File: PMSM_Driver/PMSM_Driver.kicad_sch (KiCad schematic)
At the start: 112 parts, among them J1 Screw_Terminal_01x03, J2 Screw_Terminal_01x12, Q1 RGCL60TK60, Q10 RGCL60TK60, Q11 RGCL60TK60, Q12 RGCL60TK60, Q2 RGCL60TK60, Q3 RGCL60TK60, Q4 RGCL60TK60, Q5 RGCL60TK60, Q6 RGCL60TK60, Q7 RGCL60TK60, Q8 RGCL60TK60, Q9 RGCL60TK60, U1 HCPL-3120, U10 HCPL-3120, U11 HCPL-3120, U12 HCPL-3120, U2 HCPL-3120, U3 HCPL-3120, U4 HCPL-3120, U5 HCPL-3120, U6 HCPL-3120, U7 HCPL-3120, U8 HCPL-3120, U9 HCPL-3120

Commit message: modified the schematic and PCB layout, updated datasheet and BOM
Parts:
- removed C14: 10n, Capacitor_SMD:C_0402_1005Metric, symbol Device:C_Polarized_Small
- removed C15, C18: 0.1u, Capacitor_SMD:C_0402_1005Metric, symbol Device:C_Polarized_Small
- removed D1, D13, D14, D2, D7, D8: DIODE, Package_TO_SOT_SMD:TO-263-2, symbol pspice:DIODE
- removed D10, D11, D12, D15, D16, D17, D18, D3, D4, D5, D6, D9: DIODE, Package_TO_SOT_SMD:TO-263-2, symbol Simulation_SPICE:DIODE
- removed J2: Screw_Terminal_01x12, TerminalBlock_Phoenix:TerminalBlock_Phoenix_PT-1,5-12-3.5-H_1x12_P3.50mm_Horizontal, symbol Connector:Screw_Terminal_01x12
- removed R4, R5: 500, Resistor_SMD:R_0603_1608Metric, symbol Device:R_Small
- removed R7: 10, Resistor_SMD:R_0603_1608Metric, symbol Device:R_Small
- removed U1, U11, U2, U5, U6, U7, U8, U9: HCPL-3120, Package_DIP:DIP-8_W7.62mm_SMDSocket_SmallPads, symbol Driver_FET:HCPL-3120
- added C1, C10, C2, C27, C28, C29, C30, C31, C32, C33, C34, C35, C36, C37, C38, C39, C40, C41, C42, C43, C44, C45, C46, C47, C48, C49, C50, C51, C52, C53, C54, C55, C56, C57, C58, C59, C60, C61, C62, C63, C64, C65, C66, C67, C68, C69, C70, C71, C72, C73, C74, C75, C76, C77, C78, C79, C80, C81: 1u, Capacitor_SMD:C_0402_1005Metric, symbol Device:C_Polarized_Small
- added C82, C83, C84: 1n, Capacitor_SMD:C_0603_1608Metric, symbol Device:C_Polarized
- added C85, C86, C87: 0.1u, Capacitor_SMD:C_0402_1005Metric, symbol Device:C_Polarized_Small
- added J10, J11, J12, J13, J14, J15, J16, J2, J6, J7, J8, J9: AFBR-2624Z, OptoDevice:Broadcom_AFBR-16xxZ_Horizontal, symbol Fiber_Optic:AFBR-2624Z
- added J17, J18, J5: AFBR-1624Z, OptoDevice:Broadcom_AFBR-16xxZ_Horizontal, symbol Fiber_Optic:AFBR-1624Z
- added J3: Screw_Terminal_01x02, FYP_Components:8PCV-02-006, symbol Connector:Screw_Terminal_01x02
- added J4: Screw_Terminal_01x02, TerminalBlock_Phoenix:TerminalBlock_Phoenix_MKDS-1,5-2-5.08_1x02_P5.08mm_Horizontal, symbol Connector:Screw_Terminal_01x02
- added Q1, Q10, Q15, Q2, Q20, Q21, Q22, Q23, Q24, Q3, Q4, Q9: BC846, Package_TO_SOT_SMD:SOT-23, symbol Transistor_BJT:BC846
- added R1, R2, R6: 270, Resistor_SMD:R_0603_1608Metric, symbol Device:R_Small
- added R39, R40, R41: 4.7k, Resistor_SMD:R_0402_1005Metric, symbol Device:R_Small
- added U1, U13, U14, U15, U22, U23, U24, U31, U32, U4, U5, U6: 74LVC1G04, Package_TO_SOT_SMD:SOT-23-5, symbol 74xGxx:74LVC1G04
- added U16, U17, U18, U2, U25, U26, U27, U33, U34, U7, U8, U9: MGJ2D051515SC, Converter_DCDC:Converter_DCDC_Murata_MGJ2DxxxxxxSC_THT, symbol Converter_DCDC:MGJ2D051515SC
- added U19, U20, U21, U28, U29, U30, U35, U36: HCPL-3120, Package_DIP:DIP-8_W8.89mm_SMDSocket_LongPads, symbol Driver_FET:HCPL-3120
- added U37, U38, U39, U40, U41, U42, U43, U44, U45, U46, U47, U48, U49, U50, U51, U52, U53, U54: VS-E5TH3006S2L-M3, Package_TO_SOT_SMD:TO-263-2, symbol FYP_Components:VS-E5TH3006S2L-M3
- added U55, U56, U57: ACS723xLCTR-40AB, Package_SO:SOIC-8_3.9x4.9mm_P1.27mm, symbol Sensor_Current:ACS723xLCTR-40AB
- C11, C12, C13, C19, C20, C21, C22, C4, C6: value 10n -> 1u
- C14: renamed from C1; value 4.7u -> 22u; footprint Capacitor_SMD:CP_Elec_10x10.5 -> Capacitor_SMD:CP_Elec_16x17.5
- C15: renamed from C2; value 4.7u -> 22u; footprint Capacitor_SMD:CP_Elec_10x10.5 -> Capacitor_SMD:CP_Elec_16x17.5
- C16, C17, C23, C24, C25, C26, C7, C8, C9: value 0.1u -> 1u
- C18: renamed from C10; value 0.1u -> 1u
- C3, C5: value 10n -> 0.1u
- R10, R19, R20, R33, R34, R8, R9: value 10 -> 270
- R11, R24, R25, R26, R35, R36: value 1000 -> 270; footprint Resistor_SMD:R_1206_3216Metric -> Resistor_SMD:R_0603_1608Metric
- R12, R13, R14, R23, R37, R38: value 1000 -> 10; footprint Resistor_SMD:R_1206_3216Metric -> Resistor_SMD:R_0603_1608Metric
- R15, R16, R17, R18, R27, R28, R29: value 500 -> 270
- R3, R30: value 500 -> 10
- R7: renamed from R6; value 500 -> 270
- U10, U12, U3: footprint Package_DIP:DIP-8_W7.62mm_SMDSocket_SmallPads -> Package_DIP:DIP-8_W8.89mm_SMDSocket_LongPads
- U11: renamed from U4; footprint Package_DIP:DIP-8_W7.62mm_SMDSocket_SmallPads -> Package_DIP:DIP-8_W8.89mm_SMDSocket_LongPads
- renumbered Q5 to Q11, Q6 to Q12, Q7 to Q13, Q8 to Q14, Q9 to Q16, Q10 to Q17, Q11 to Q18, Q12 to Q19, Q1 to Q5, Q2 to Q6, Q3 to Q7, Q4 to Q8, R1 to R4, R2 to R5
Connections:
- net +BATT: now also J3.1 (Pin_1), U43.2 (C), U47.2 (C), U51.2 (C)
- net -BATT: now also C57.2, C63.2, C69.2, C71.2, C73.2, C75.2, C77.2, C79.2, C81.2, J3.2 (Pin_2), U27.5 (-VOUT), U30.5 (VEE), U33.5 (-VOUT), U34.5 (-VOUT), U35.5 (VEE), U36.5 (VEE), U46.1 (N/C), U46.3 (A), U50.1 (N/C), U50.3 (A), U54.1 (N/C), U54.3 (A)
- net A1: now also Q5.1 (G), R13.2; no longer R10.2, R14.1, U11.6 (VO), U11.7 (VO)
- net A2: now also Q6.1 (G), R22.2; no longer R13.1, R9.2, U3.6 (VO), U3.7 (VO)
- net A3: now also Q7.1 (G), R31.2; no longer R11.1, R8.2
- net A4: now also Q8.1 (G), R38.2; no longer R12.1
- net B1: now also Q11.1 (G), R12.2; no longer R22.2, R24.1
- net B2: now also Q12.1 (G); no longer R23.1
- net B3: now also Q13.1 (G), R30.2; no longer R20.2, R25.1
- net B4: now also Q14.1 (G), R37.2; no longer R19.2, R26.1
- net C1: now also Q16.1 (G), R3.2; no longer R34.2, R36.1, U12.6 (VO), U12.7 (VO)
- net C2: now also Q17.1 (G), R14.2; no longer R33.2, R37.1
- net C3: now also Q18.1 (G), R23.2; no longer R32.2, R38.1, U10.6 (VO), U10.7 (VO)
- net C4: now also Q19.1 (G), R32.2; no longer R31.2, R35.1
- net GND: now also C1.2, C2.2, C82.2, C83.2, C84.2, C85.2, C86.2, C87.2, J10.2 (VEER), J10.5 (HP), J10.8 (HP), J11.2 (VEER), J11.5 (HP), J11.8 (HP), J12.2 (VEER), J12.5 (HP), J12.8 (HP), J13.2 (VEER), J13.5 (HP), J13.8 (HP), J14.2 (VEER), J14.5 (HP), J14.8 (HP), J15.2 (VEER), J15.5 (HP), J15.8 (HP), J16.2 (VEER), J16.5 (HP), J16.8 (HP), J17.3 (VEET), J17.5 (HP), J17.8 (HP), J18.3 (VEET), J18.5 (HP), J18.8 (HP), J2.2 (VEER), J2.5 (HP), J2.8 (HP), J4.2 (Pin_2), J5.3 (VEET), J5.5 (HP), J5.8 (HP), J6.2 (VEER), J6.5 (HP), J6.8 (HP), J7.2 (VEER), J7.5 (HP), J7.8 (HP), J8.2 (VEER), J8.5 (HP), J8.8 (HP), J9.2 (VEER), J9.5 (HP), J9.8 (HP), R39.2, R40.2, R41.2, U1.3 (GND), U13.3 (GND), U14.3 (GND), U15.3 (GND), U16.2 (-VIN), U17.2 (-VIN), U18.2 (-VIN), U2.2 (-VIN), U22.3 (GND), U23.3 (GND), U24.3 (GND), U25.2 (-VIN), U26.2 (-VIN), U27.2 (-VIN), U31.3 (GND), U32.3 (GND), U33.2 (-VIN), U34.2 (-VIN), U4.3 (GND), U5.3 (GND), U55.5 (GND), U55.6 (BW_SEL), U56.5 (GND), U56.6 (BW_SEL), U57.5 (GND), U57.6 (BW_SEL), U6.3 (GND), U7.2 (-VIN), U8.2 (-VIN), U9.2 (-VIN); no longer C11.2, C12.2, C13.2, C16.2, C17.2, C18.2, C19.2, C20.2, C21.2, C22.2, C23.2, C24.2, C25.2, C26.2, C7.2, C8.2, U10.5 (VEE), U11.5 (VEE), U12.5 (VEE), U3.5 (VEE)
- net GNDD: now also Q1.2 (E), Q10.2 (E), Q15.2 (E), Q2.2 (E), Q20.2 (E), Q21.2 (E), Q22.2 (E), Q23.2 (E), Q24.2 (E), Q3.2 (E), Q4.2 (E), Q9.2 (E), U19.3 (C), U20.3 (C), U21.3 (C), U28.3 (C), U29.3 (C), U30.3 (C), U35.3 (C), U36.3 (C)
- net GNDREF: now also U37.1 (N/C), U37.3 (A), U38.2 (C), U39.1 (N/C), U39.3 (A), U40.2 (C), U41.1 (N/C), U41.3 (A), U42.2 (C)
- net ia_out: now also C37.2, C41.2, C47.2, U17.5 (-VOUT), U20.5 (VEE), U44.1 (N/C), U44.3 (A), U45.2 (C), U55.1 (IP+), U55.2 (IP+); no longer J1.3 (Pin_3)
- net ib_out: now also C35.2, C39.2, C45.2, U16.5 (-VOUT), U19.5 (VEE), U48.1 (N/C), U48.3 (A), U49.2 (C), U56.1 (IP+), U56.2 (IP+); no longer J1.2 (Pin_2)
- net ic_out: now also C21.2, U12.5 (VEE), C27.2, C33.2, U52.1 (N/C), U52.3 (A), U53.2 (C), U57.1 (IP+), U57.2 (IP+), U9.5 (-VOUT); no longer J1.1 (Pin_1)
- net at R20.1: now also Q15.3 (C), U21.2 (A); no longer C12.1
- net -15V_B1: now reaches Q11.3 (E), Q12.2 (C)
- net -15V_B1: now also C17.2, C23.2, U10.5 (VEE), C29.2, U39.2 (C), U47.1 (N/C), U47.3 (A), U48.2 (C), U7.5 (-VOUT)
- net -15V_C3: now reaches Q18.3 (E), Q19.2 (C)
- net -15V_C3: now also C43.2, C49.2, C51.2, U18.5 (-VOUT), U21.5 (VEE), U42.1 (N/C), U42.3 (A), U53.1 (N/C), U53.3 (A), U54.2 (C)
- net at R31.1: now also U29.6 (VO), U29.7 (VO); no longer C19.1
- net +5V: now reaches R35.2
- net +5V: now also C3.1, C4.1, C5.1, C6.1, C9.1, R10.2, R11.2, R18.2, R19.2, R20.2, R27.2, R28.2, R29.2, R36.2, R9.2, C1.1, C2.1, J10.3 (VCCR), J11.3 (VCCR), J12.3 (VCCR), J13.3 (VCCR), J14.3 (VCCR), J15.3 (VCCR), J16.3 (VCCR), J17.1 (VCCT), J18.1 (VCCT), J2.3 (VCCR), J4.1 (Pin_1), J5.1 (VCCT), J6.3 (VCCR), J7.3 (VCCR), J8.3 (VCCR), J9.3 (VCCR), R2.2, U1.5 (VCC), U13.5 (VCC), U14.5 (VCC), U15.5 (VCC), U16.1 (+VIN), U17.1 (+VIN), U18.1 (+VIN), U2.1 (+VIN), U22.5 (VCC), U23.5 (VCC), U24.5 (VCC), U25.1 (+VIN), U26.1 (+VIN), U27.1 (+VIN), U31.5 (VCC), U32.5 (VCC), U33.1 (+VIN), U34.1 (+VIN), U4.5 (VCC), U5.5 (VCC), U55.8 (VCC), U56.8 (VCC), U57.8 (VCC), U6.5 (VCC), U7.1 (+VIN), U8.1 (+VIN), U9.1 (+VIN); no longer Q19.1 (G)
- net at R22.1: now also U20.6 (VO), U20.7 (VO)
- net -15V_C1: now reaches Q16.3 (E), Q17.2 (C)
- net -15V_C1: now also C11.2, C13.2, C8.2, U3.5 (VEE), U2.5 (-VOUT), U41.2 (C), U51.1 (N/C), U51.3 (A), U52.2 (C)
- net at C13.1: now also C11.1, C12.2, C7.2, C8.1, C10.2, U2.6 (0V); no longer R21.1
- net at R32.1: now also U30.6 (VO), U30.7 (VO); no longer C20.1
- net at C21.1: now also C20.2, C26.2, C27.1, C32.2, C33.1, U9.6 (0V); no longer R33.1
- net -15V_A3: now reaches Q7.3 (E), Q8.2 (C)
- net -15V_A3: now also C55.2, C61.2, C67.2, U26.5 (-VOUT), U29.5 (VEE), U38.1 (N/C), U38.3 (A), U45.1 (N/C), U45.3 (A), U46.2 (C)
- net at R9.1: now also U10.2 (A), Q2.3 (C); no longer C5.1
- net -15V_A1: now reaches Q5.3 (E), Q6.2 (C)
- net -15V_A1: now also C19.2, C25.2, U11.5 (VEE), C31.2, U37.2 (C), U43.1 (N/C), U43.3 (A), U44.2 (C), U8.5 (-VOUT)
- net at R15.2: now also Q9.1 (B)
- net -15V_B3: now reaches Q13.3 (E), Q14.2 (C)
- net -15V_B3: now also C53.2, C59.2, C65.2, U25.5 (-VOUT), U28.5 (VEE), U40.1 (N/C), U40.3 (A), U49.1 (N/C), U49.3 (A), U50.2 (C)
- net at R26.2: now also Q22.1 (B); no longer Q14.1 (G)
- net at R8.1: now also U6.4; no longer C4.1
- net at R24.2: now also Q20.1 (B); no longer Q11.1 (G)
- net at R19.1: now also Q10.3 (C), U20.2 (A); no longer C11.1
- net at U11.2 (A): now also R10.1, Q3.3 (C); no longer R7.2
- net at R17.2: now also Q15.1 (B)
- net at R25.2: now also Q21.1 (B); no longer Q13.1 (G)
- net at U12.2 (A): now also R11.1, Q4.3 (C); no longer R30.2
- net at U3.2 (A): now also Q1.3 (C), R2.1
- net at R34.1: now also U32.4; no longer C22.1
- net at R16.2: now also Q10.1 (B)
- net PWM_A1: no longer names the net of R7.1
- net PWM_A1: now also U5.4
- net PWM_A4: no longer names the net of R3.1
- net PWM_A4: now also U3.6 (VO), U3.7 (VO)
- net PWM_B1: no longer names the net of R18.1
- net PWM_B1: now also Q9.3 (C), U19.2 (A)
- net PWM_B2: no longer names the net of R17.1
- net PWM_B2: now also U15.4
- net PWM_B3: no longer names the net of R16.1
- net PWM_B3: now also U14.4
- net PWM_B4: no longer names the net of R15.1
- net PWM_B4: now also U13.4
- net PWM_C1: no longer names the net of R30.1
- net PWM_C1: now also U28.6 (VO), U28.7 (VO)
- net PWM_C2: no longer names the net of R29.1
- net PWM_C2: now also Q22.3 (C), U30.2 (A)
- net PWM_C3: no longer names the net of R28.1
- net PWM_C3: now also Q21.3 (C), U29.2 (A)
- net PWM_C4: no longer names the net of R27.1
- net PWM_C4: now also Q20.3 (C), U28.2 (A)
- removed net VCC: C16.1, C17.1, C18.1, C23.1, C24.1, C25.1, C26.1, C7.1, C8.1, C9.1, U10.8 (VCC), U11.8 (VCC), U12.8 (VCC), U3.8 (VCC)
- new net: C42.2, C43.1, C48.2, C49.1, C50.2, C51.1, U18.6 (0V)
- new net: C54.2, C55.1, C60.2, C61.1, C66.2, C67.1, U26.6 (0V)
- new net: C16.2, C17.1, C22.2, C23.1, C28.2, C29.1, U7.6 (0V)
- new net: J10.1 (Data_Out), U6.2
- new net: C36.2, C37.1, C40.2, C41.1, C46.2, C47.1, U17.6 (0V)
- new net: C52.2, C53.1, C58.2, C59.1, C64.2, C65.1, U25.6 (0V)
- new net: J7.1 (Data_Out), U1.2
- new net: R1.1, U1.4
- new net: C18.2, C19.1, C24.2, C25.1, C30.2, C31.1, U8.6 (0V)
- new net: C34.2, C35.1, C38.2, C39.1, C44.2, C45.1, U16.6 (0V)
- new net: R14.1, U12.6 (VO), U12.7 (VO)
- new net: Q23.3 (C), R35.1, U35.2 (A)
- new net: J9.1 (Data_Out), U13.2
- new net: J8.1 (Data_Out), U14.2
- new net: J15.1 (Data_Out), U31.2
- new net: J12.1 (Data_Out), U22.2
- new net: R24.1, U22.4
- new net: C70.2, C71.1, C74.2, C75.1, C78.2, C79.1, U33.6 (0V)
- new net: R21.1, U19.6 (VO), U19.7 (VO)
- new net: C72.2, C73.1, C76.2, C77.1, C80.2, C81.1, U34.6 (0V)
- new net: R33.1, U31.4
- new net: C56.2, C57.1, C62.2, C63.1, C68.2, C69.1, U27.6 (0V)
- new net: J14.1 (Data_Out), U32.2
- new net: Q3.1 (B), R7.2
- new net: J13.1 (Data_Out), U15.2
- new net: J6.1 (Data_Out), U5.2
- new net: J2.1 (Data_Out), U4.2
- new net: R6.1, U4.4
- new net: R12.1, U10.6 (VO), U10.7 (VO)
- new net: R13.1, U11.6 (VO), U11.7 (VO)
- new net: R38.1, U36.6 (VO), U36.7 (VO)
- new net: J11.1 (Data_Out), U23.2
- new net: R25.1, U23.4
- new net: R26.1, U24.4
- new net: Q4.1 (B), R8.2
- new net: Q1.1 (B), R1.2
- new net: Q24.1 (B), R34.2
- new net: R37.1, U35.6 (VO), U35.7 (VO)
- new net: Q23.1 (B), R33.2
- new net: Q2.1 (B), R6.2
- new net: J16.1 (Data_Out), U24.2
- new net: Q24.3 (C), R36.1, U36.2 (A)
- new net: R23.1, U21.6 (VO), U21.7 (VO)
- new net +15V_A1: C18.1, C24.1, C30.1, U11.8 (VCC), U8.7 (+VOUT)
- new net +15V_A2: C36.1, C40.1, C46.1, U17.7 (+VOUT), U20.8 (VCC)
- new net +15V_A3: C54.1, C60.1, C66.1, U26.7 (+VOUT), U29.8 (VCC)
- new net +15V_A4: C72.1, C76.1, C80.1, U34.7 (+VOUT), U36.8 (VCC)
- new net +15V_B1: C16.1, C22.1, C28.1, U10.8 (VCC), U7.7 (+VOUT)
- new net +15V_B2: C34.1, C38.1, C44.1, U16.7 (+VOUT), U19.8 (VCC)
- new net +15V_B3: C52.1, C58.1, C64.1, U25.7 (+VOUT), U28.8 (VCC)
- new net +15V_B4: C70.1, C74.1, C78.1, U33.7 (+VOUT), U35.8 (VCC)
- new net +15V_C1: C10.1, C12.1, C7.1, U2.7 (+VOUT), U3.8 (VCC)
- new net +15V_C2: C20.1, C26.1, C32.1, U12.8 (VCC), U9.7 (+VOUT)
- new net +15V_C3: C42.1, C48.1, C50.1, U18.7 (+VOUT), U21.8 (VCC)
- new net +15V_C4: C56.1, C62.1, C68.1, U27.7 (+VOUT), U30.8 (VCC)
- new net a_out: J1.1 (Pin_1), U55.3 (IP-), U55.4 (IP-)
- new net b_out: J1.2 (Pin_2), U56.3 (IP-), U56.4 (IP-)
- new net c_out: J1.3 (Pin_3), U57.3 (IP-), U57.4 (IP-)
- new net ia_signal: C82.1, C85.1, J17.4 (Data_in), R39.1, U55.7 (VIOUT)
- new net ib_signal: C83.1, C86.1, J5.4 (Data_in), R40.1, U56.7 (VIOUT)
- new net ic_signal: C84.1, C87.1, J18.4 (Data_in), R41.1, U57.7 (VIOUT)
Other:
- note added: "Current Sensor"
- note added: "Gate Drive"
- note added: "Power Supply"
- note added: "Terminals"
- note added: "Three Phase Inverter"
- moved on the sheet: C14, C15, C18, H1, H2, H3, H4, J1, Q11, Q12, Q13, Q14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

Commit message: update on PCB layout
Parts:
- removed J1: Screw_Terminal_01x03, TerminalBlock_Phoenix:TerminalBlock_Phoenix_MKDS-1,5-3-5.08_1x03_P5.08mm_Horizontal, symbol Connector:Screw_Terminal_01x03
- removed J3: Screw_Terminal_01x02, FYP_Components:8PCV-02-006, symbol Connector:Screw_Terminal_01x02
- removed J4: Screw_Terminal_01x02, TerminalBlock_Phoenix:TerminalBlock_Phoenix_MKDS-1,5-2-5.08_1x02_P5.08mm_Horizontal, symbol Connector:Screw_Terminal_01x02
- added J1: 1714984, FYP_Components:CONN_1714984_PXC, symbol FYP_Components:1714984
- added J3, J4: 1714971, FYP_Components:CONN_1714971_PXC, symbol FYP_Components:1714971
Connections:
- net GNDD is gone; now on net GND: Q1.2 (E), Q10.2 (E), Q15.2 (E), Q2.2 (E), Q20.2 (E), Q21.2 (E), Q22.2 (E), Q23.2 (E), Q24.2 (E), Q3.2 (E), Q4.2 (E), Q9.2 (E), U10.3 (C), U11.3 (C), U12.3 (C), U19.3 (C), U20.3 (C), U21.3 (C), U28.3 (C), U29.3 (C), U3.3 (C), U30.3 (C), U35.3 (C), U36.3 (C)
- net +5V: now also J4.1
- net +BATT: now also J3.1
- net -15V_A1: no longer Q5.3 (E), Q6.2 (C), U37.2 (C), U43.1 (N/C), U43.3 (A), U44.2 (C)
- net -15V_A3: no longer Q7.3 (E), Q8.2 (C), U38.1 (N/C), U38.3 (A), U45.1 (N/C), U45.3 (A), U46.2 (C)
- net -15V_B1: no longer Q11.3 (E), Q12.2 (C), U39.2 (C), U47.1 (N/C), U47.3 (A), U48.2 (C)
- net -15V_B3: no longer Q13.3 (E), Q14.2 (C), U40.1 (N/C), U40.3 (A), U49.1 (N/C), U49.3 (A), U50.2 (C)
- net -15V_C1: no longer Q16.3 (E), Q17.2 (C), U41.2 (C), U51.1 (N/C), U51.3 (A), U52.2 (C)
- net -15V_C3: no longer Q18.3 (E), Q19.2 (C), U42.1 (N/C), U42.3 (A), U53.1 (N/C), U53.3 (A), U54.2 (C)
- net -BATT: now also C56.2, C57.1, C62.2, C63.1, C68.2, C69.1, C70.2, C71.1, C72.2, C73.1, C74.2, C75.1, C76.2, C77.1, C78.2, C79.1, C80.2, C81.1, U27.6 (0V), U33.6 (0V), U34.6 (0V), J3.2; no longer C57.2, C63.2, C69.2, C71.2, C73.2, C75.2, C77.2, C79.2, C81.2, U27.5 (-VOUT), U30.5 (VEE), U33.5 (-VOUT), U34.5 (-VOUT), U35.5 (VEE), U36.5 (VEE)
- net GND: now also J4.2
- net a_out: now also J1.1
- net b_out: now also J1.2
- net c_out: now also J1.3
- net ia_out: now also C36.2, C37.1, C40.2, C41.1, C46.2, C47.1, U17.6 (0V); no longer C37.2, C41.2, C47.2, U17.5 (-VOUT), U20.5 (VEE)
- net ib_out: now also C34.2, C35.1, C38.2, C39.1, C44.2, C45.1, U16.6 (0V); no longer C35.2, C39.2, C45.2, U16.5 (-VOUT), U19.5 (VEE)
- net ic_out: now also C20.2, C21.1, C26.2, C27.1, C32.2, C33.1, U9.6 (0V); no longer C21.2, C27.2, C33.2, U12.5 (VEE), U9.5 (-VOUT)
- net C1_E: now reaches C10.2, C11.1, C12.2, C13.1, C7.2, C8.1, U2.6 (0V)
- net C1_E: now also Q16.3 (E), Q17.2 (C), U41.2 (C), U51.1 (N/C), U51.3 (A), U52.2 (C)
- net C3_E: now reaches C42.2, C43.1, C48.2, C49.1, C50.2, C51.1, U18.6 (0V)
- net C3_E: now also Q18.3 (E), Q19.2 (C), U42.1 (N/C), U42.3 (A), U53.1 (N/C), U53.3 (A), U54.2 (C)
- net A3_E: now reaches C54.2, C55.1, C60.2, C61.1, C66.2, C67.1, U26.6 (0V)
- net A3_E: now also Q7.3 (E), Q8.2 (C), U38.1 (N/C), U38.3 (A), U45.1 (N/C), U45.3 (A), U46.2 (C)
- net B1_E: now reaches C16.2, C17.1, C22.2, C23.1, C28.2, C29.1, U7.6 (0V)
- net B1_E: now also Q11.3 (E), Q12.2 (C), U39.2 (C), U47.1 (N/C), U47.3 (A), U48.2 (C)
- net B3_E: now reaches C52.2, C53.1, C58.2, C59.1, C64.2, C65.1, U25.6 (0V)
- net B3_E: now also Q13.3 (E), Q14.2 (C), U40.1 (N/C), U40.3 (A), U49.1 (N/C), U49.3 (A), U50.2 (C)
- net A1_E: now reaches C18.2, C19.1, C24.2, C25.1, C30.2, C31.1, U8.6 (0V)
- net A1_E: now also Q5.3 (E), Q6.2 (C), U37.2 (C), U43.1 (N/C), U43.3 (A), U44.2 (C)
- new net -15V_A2: C37.2, C41.2, C47.2, U17.5 (-VOUT), U20.5 (VEE)
- new net -15V_A4: C73.2, C77.2, C81.2, U34.5 (-VOUT), U36.5 (VEE)
- new net -15V_B2: C35.2, C39.2, C45.2, U16.5 (-VOUT), U19.5 (VEE)
- new net -15V_B4: C71.2, C75.2, C79.2, U33.5 (-VOUT), U35.5 (VEE)
- new net -15V_C2: C21.2, C27.2, C33.2, U12.5 (VEE), U9.5 (-VOUT)
- new net -15V_C4: C57.2, C63.2, C69.2, U27.5 (-VOUT), U30.5 (VEE)
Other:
- moved on the sheet: C12, C13, C28, C29, C30, C31, C32, C33, C42, C43, C44, C45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

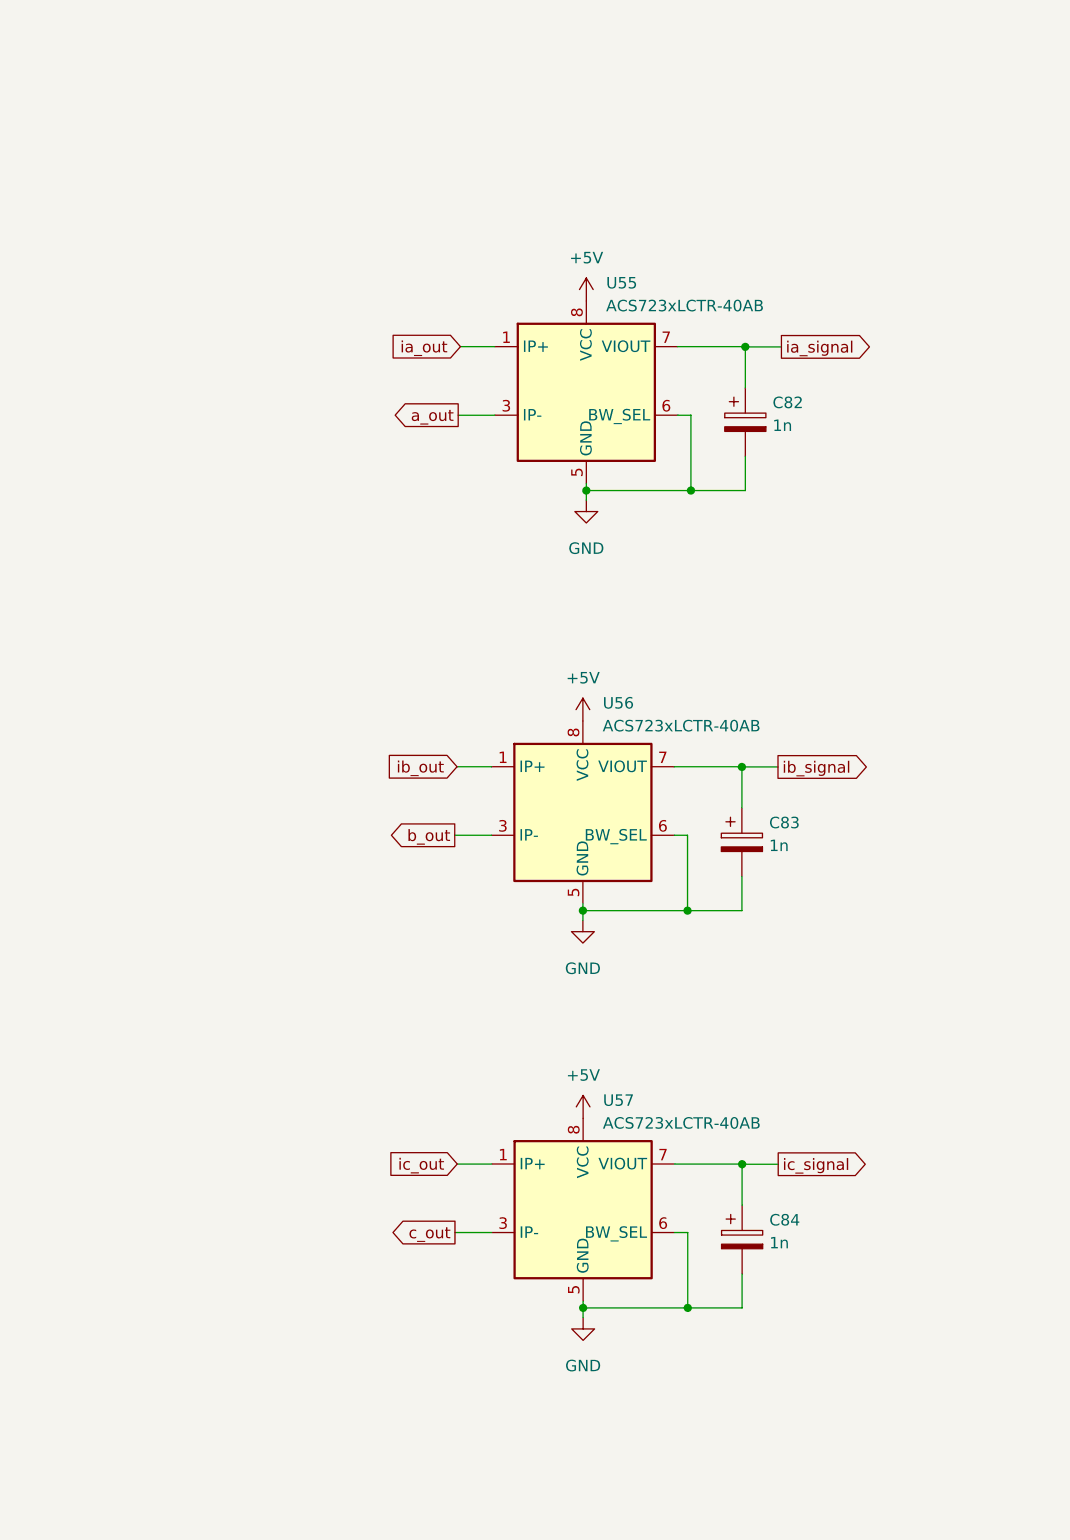
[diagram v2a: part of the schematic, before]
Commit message: add single buffers to signal output, update layout
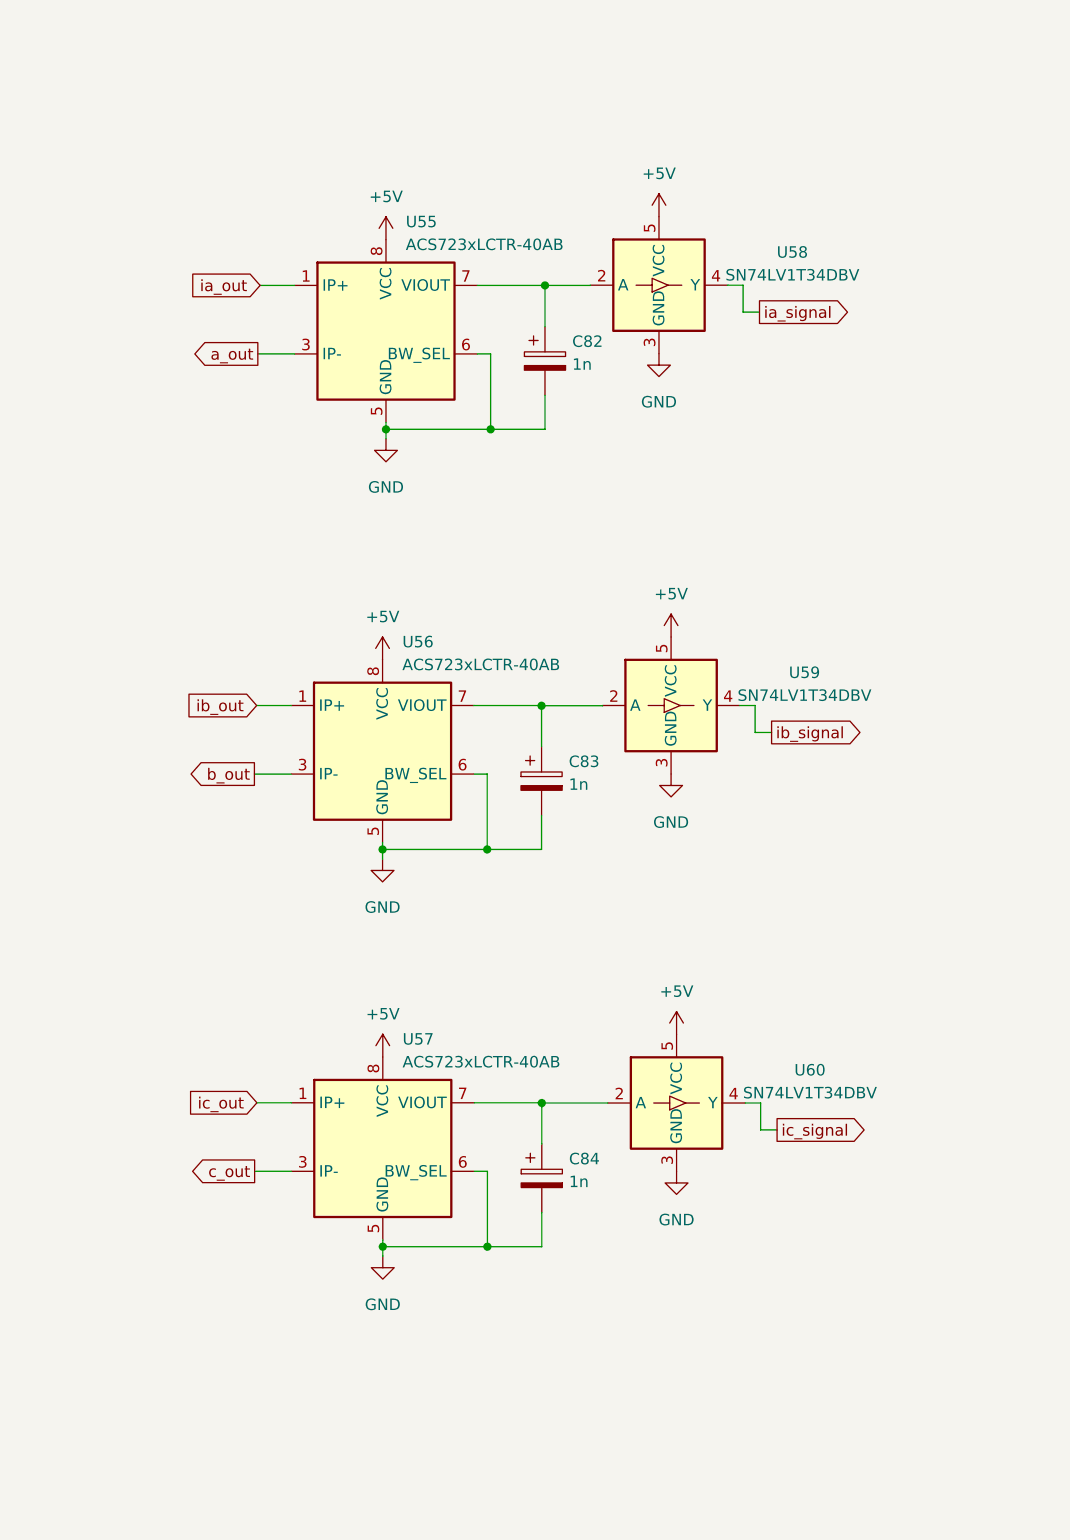
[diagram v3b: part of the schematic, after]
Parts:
- added U58, U59, U60: SN74LV1T34DBV, Package_TO_SOT_SMD:SOT-23-5, symbol Logic_LevelTranslator:SN74LV1T34DBV
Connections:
- net +5V: now also U58.5 (VCC), U59.5 (VCC), U60.5 (VCC)
- net GND: now also U58.3 (GND), U59.3 (GND), U60.3 (GND)
- net ia_signal: now also U58.4 (Y); no longer C82.1, U55.7 (VIOUT)
- net ib_signal: now also U59.4 (Y); no longer C83.1, U56.7 (VIOUT)
- net ic_signal: now also U60.4 (Y); no longer C84.1, U57.7 (VIOUT)
- new net: C84.1, U57.7 (VIOUT), U60.2 (A)
- new net: C82.1, U55.7 (VIOUT), U58.2 (A)
- new net: C83.1, U56.7 (VIOUT), U59.2 (A)
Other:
- moved on the sheet: C82, C83, C84, U55, U56, U57

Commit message: modified single buffer to voltage follower, modification on gate drive protection circuit is needed
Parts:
- removed C85, C86, C87: 0.1u, Capacitor_SMD:C_0402_1005Metric, symbol Device:C_Polarized_Small
- removed J17, J18, J5: AFBR-1624Z, OptoDevice:Broadcom_AFBR-16xxZ_Horizontal, symbol Fiber_Optic:AFBR-1624Z
- removed R39, R40, R41: 4.7k, Resistor_SMD:R_0402_1005Metric, symbol Device:R_Small
- removed U58, U59, U60: SN74LV1T34DBV, Package_TO_SOT_SMD:SOT-23-5, symbol Logic_LevelTranslator:SN74LV1T34DBV
- added J5: 1827907, FYP_Components:CONN_1827907, symbol FYP_Components:1827907
- added U58, U59, U60: LMV641MF/NOPB, FYP_Components:DBV5_TEX, symbol FYP_Components:LMV641MF_NOPB
- R4, R5: value 100M -> 20k
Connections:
- net +5V: now also U58.5 (V+), U59.5 (V+), U60.5 (V+)
- net GND: now also J5.2, J5.4, J5.6, U58.2 (V-), U59.2 (V-), U60.2 (V-)
- net ia_signal: now also J5.1, U58.1 (VOUT), U58.4 (VIN-)
- net ib_signal: now also J5.3, U59.1 (VOUT), U59.4 (VIN-)
- net ic_signal: now also J5.5, U60.1 (VOUT), U60.4 (VIN-)
- net at C84.1, U57.7 (VIOUT): now also U60.3 (VIN+)
- net at C82.1, U55.7 (VIOUT): now also U58.3 (VIN+)
- net at C83.1, U56.7 (VIOUT): now also U59.3 (VIN+)
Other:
- moved on the sheet: C82, H1, H2, H3, H4, J1, J4, U55

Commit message: updated PCB layout: gate drive protection
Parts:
- added D1, D10, D11, D12, D13, D14, D15, D16, D17, D18, D19, D2, D20, D21, D22, D23, D24, D3, D4, D5, D6, D7, D8, D9: BZX384C18, Diode_SMD:D_SOD-323, symbol Diode:BZX384xxxx
- added R39, R41, R43, R45, R47, R49, R51, R53, R55, R57, R59, R61: 50, Resistor_SMD:R_0603_1608Metric, symbol Device:R_Small
- added R40, R42, R44, R46, R48, R50, R52, R54, R56, R58, R60, R62: 20k, Resistor_SMD:R_0603_1608Metric, symbol Device:R_Small
- R12, R13, R14, R21, R22, R23, R3, R30, R31, R32, R37, R38: value 10 -> 50
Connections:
- net -BATT: now also D20.1 (K), D22.1 (K), D24.1 (K), R58.2, R60.2, R62.2
- net A1: now also D1.1 (K), R39.2, R40.1
- net A1_E: now also D2.1 (K), R40.2
- net A2: now also D7.1 (K), R45.2, R46.1
- net A3: now also D13.1 (K), R51.2, R52.1
- net A3_E: now also D14.1 (K), R52.2
- net A4: now also D19.1 (K), R57.2, R58.1
- net B1: now also D3.1 (K), R41.2, R42.1
- net B1_E: now also D4.1 (K), R42.2
- net B2: now also D9.1 (K), R47.2, R48.1
- net B3: now also D15.1 (K), R53.2, R54.1
- net B3_E: now also D16.1 (K), R54.2
- net B4: now also D21.1 (K), R59.2, R60.1
- net C1: now also D5.1 (K), R43.2, R44.1
- net C1_E: now also D6.1 (K), R44.2
- net C2: now also D11.1 (K), R49.2, R50.1
- net C3: now also D17.1 (K), R55.2, R56.1
- net C3_E: now also D18.1 (K), R56.2
- net C4: now also D23.1 (K), R61.2, R62.1
- net GND: now also J5.1, J5.3, J5.5; no longer J5.2, J5.4, J5.6
- net ia_out: now also D8.1 (K), R46.2
- net ia_signal: now also J5.6; no longer J5.1
- net ib_out: now also D10.1 (K), R48.2
- net ib_signal: now also J5.4; no longer J5.3
- net ic_out: now also D12.1 (K), R50.2
- net ic_signal: now also J5.2; no longer J5.5
- net at R31.1, U29.6 (VO), U29.7 (VO): now also R51.1
- net at R3.1, U3.6 (VO), U3.7 (VO): now also R43.1
- net at R30.1, U28.6 (VO), U28.7 (VO): now also R53.1
- net at R22.1, U20.6 (VO), U20.7 (VO): now also R45.1
- net at R14.1, U12.6 (VO), U12.7 (VO): now also R49.1
- net at R21.1, U19.6 (VO), U19.7 (VO): now also R47.1
- net at R12.1, U10.6 (VO), U10.7 (VO): now also R41.1
- net at R13.1, U11.6 (VO), U11.7 (VO): now also R39.1
- net at R38.1, U36.6 (VO), U36.7 (VO): now also R57.1
- net at R32.1, U30.6 (VO), U30.7 (VO): now also R61.1
- net at R37.1, U35.6 (VO), U35.7 (VO): now also R59.1
- net at R23.1, U21.6 (VO), U21.7 (VO): now also R55.1
- new net: D11.2 (A), D12.2 (A)
- new net: D5.2 (A), D6.2 (A)
- new net: D3.2 (A), D4.2 (A)
- new net: D1.2 (A), D2.2 (A)
- new net: D21.2 (A), D22.2 (A)
- new net: D13.2 (A), D14.2 (A)
- new net: D19.2 (A), D20.2 (A)
- new net: D7.2 (A), D8.2 (A)
- new net: D23.2 (A), D24.2 (A)
- new net: D10.2 (A), D9.2 (A)
- new net: D17.2 (A), D18.2 (A)
- new net: D15.2 (A), D16.2 (A)
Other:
- moved on the sheet: C1, C10, C11, C12, C13, C14, C15, C16, C17, C18, C19, C2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

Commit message: TBC: change trace for 10A current to filled zone
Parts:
- removed J1: 1714984, FYP_Components:CONN_1714984_PXC, symbol FYP_Components:1714984
- added J1, J17, J18: 2606-1101, FYP_Components:CONN_2606-1101_WAG, symbol FYP_Components:2606-1101
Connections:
- net a_out: now also J1.1_1, J1.1_2
- net b_out: now also J17.1_1, J17.1_2
- net c_out: now also J18.1_1, J18.1_2
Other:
- note added: "3-Phase PWM Output Voltage"
- note added: "5V Supply"
- note added: "Current Signal Output"
- note added: "DC Battery Supply"
- note added: "Decoupling Capacitors"
- note added: "Voltage Follower"
- moved on the sheet: C1, C2, C3, C4, C5, C6, C9, H1, H2, H3, H4, J3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
